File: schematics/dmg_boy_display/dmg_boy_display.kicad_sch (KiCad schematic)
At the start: 13 parts, among them J1 GAMEBOY FLEX PINS, U1 74HC4050

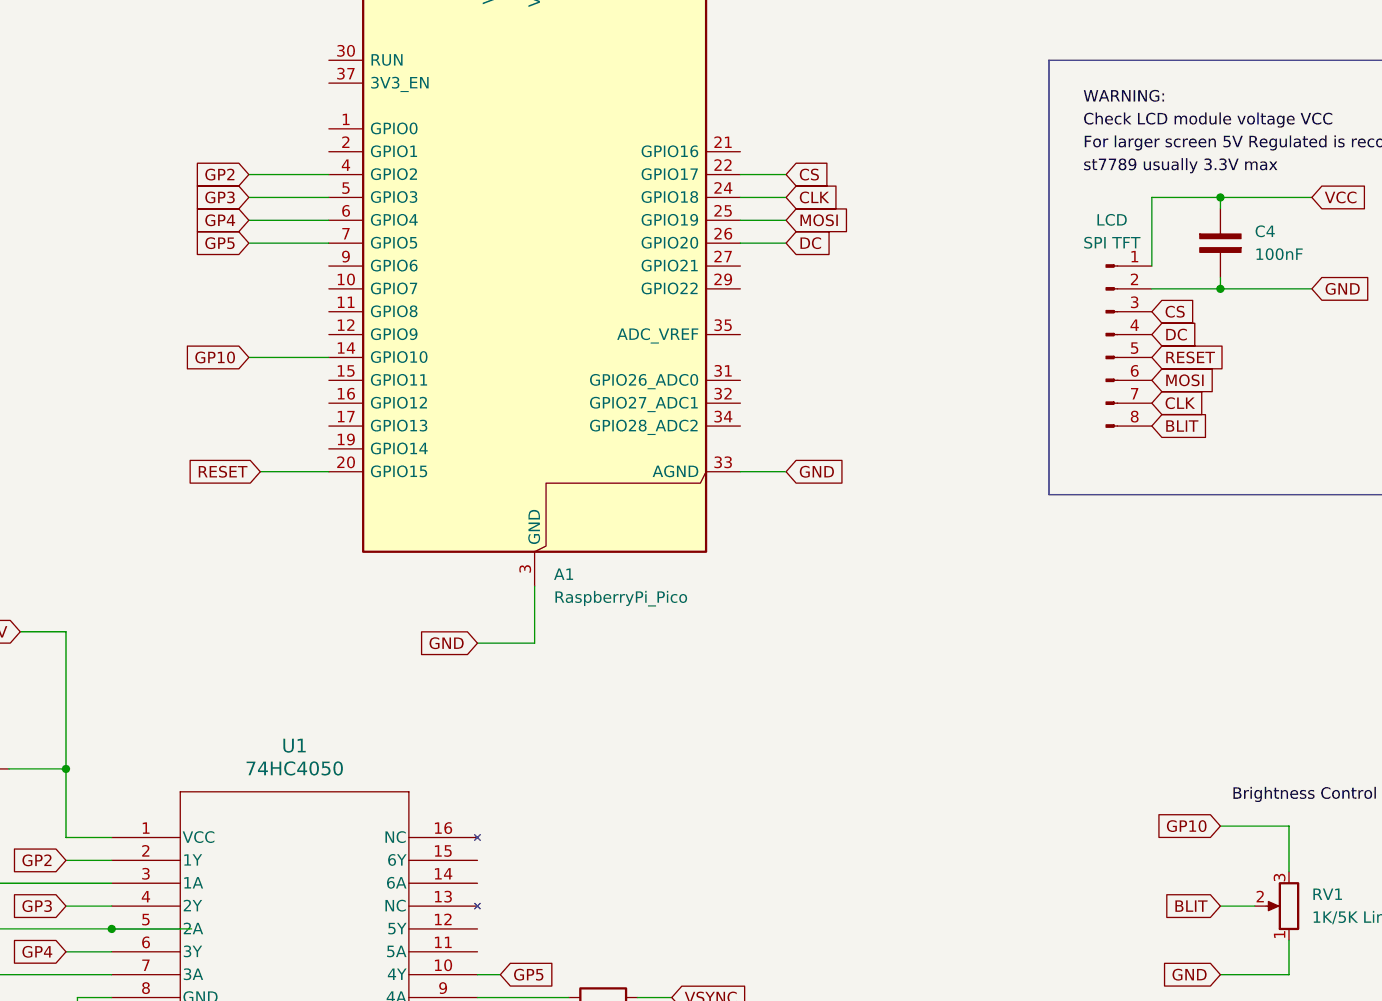
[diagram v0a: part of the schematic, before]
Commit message: change pinout for convinient and portabilty
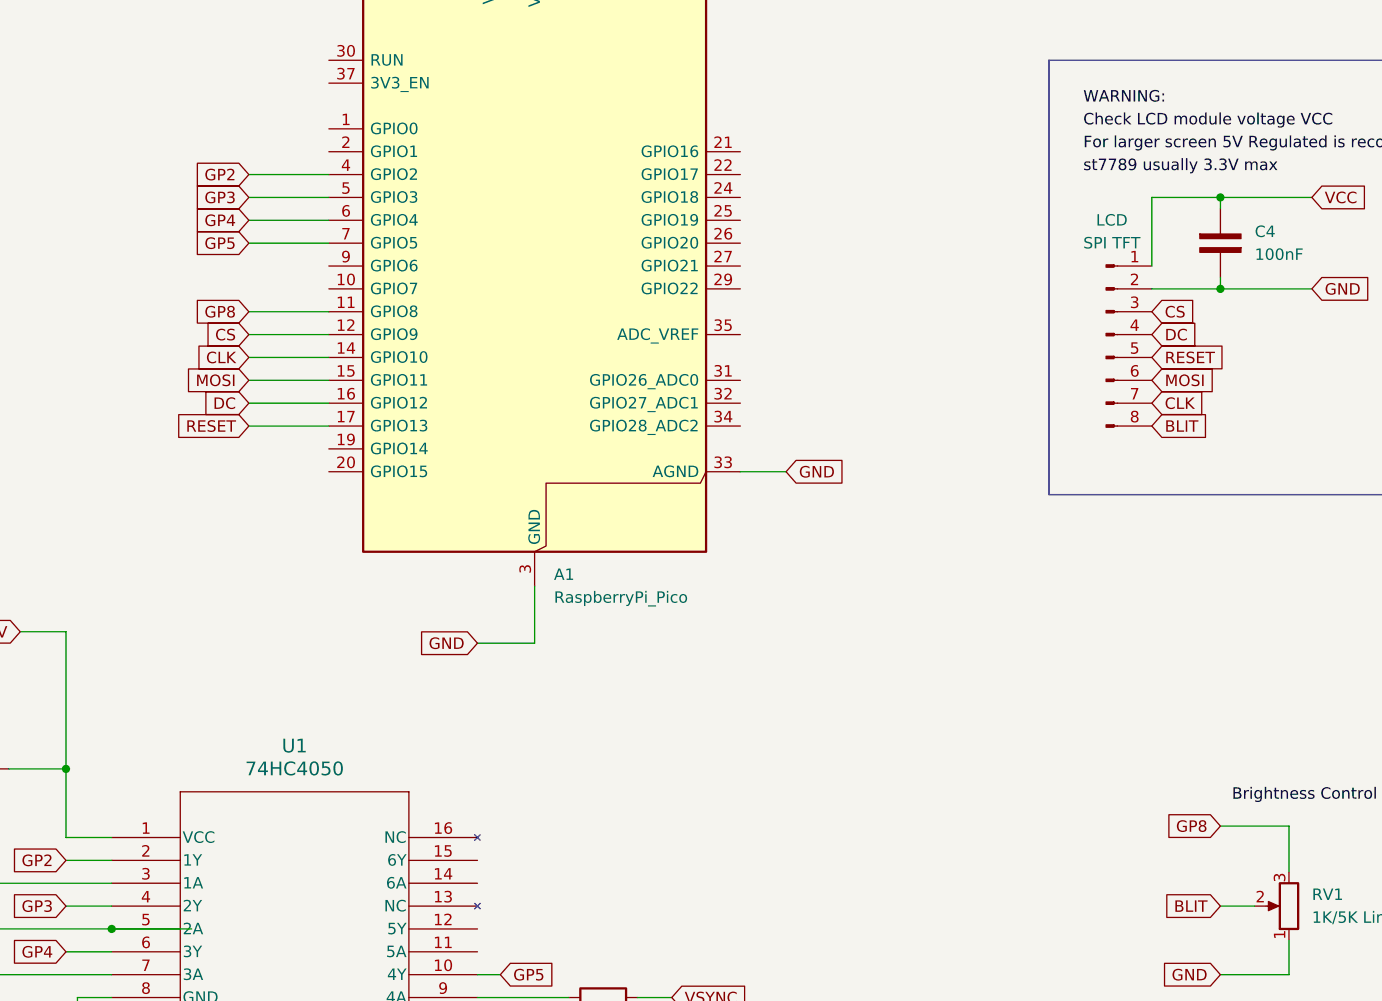
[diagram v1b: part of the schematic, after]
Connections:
- net CLK: now also A1.14 (GPIO10); no longer A1.24 (GPIO18)
- net CS: now also A1.12 (GPIO9); no longer A1.22 (GPIO17)
- net DC: now also A1.16 (GPIO12); no longer A1.26 (GPIO20)
- net MOSI: now also A1.15 (GPIO11); no longer A1.25 (GPIO19)
- net RESET: now also A1.17 (GPIO13); no longer A1.20 (GPIO15)
- net GP8: now reaches A1.11 (GPIO8)
- net GP8: now also RV1.3
- removed net GP10: A1.14 (GPIO10), RV1.3
